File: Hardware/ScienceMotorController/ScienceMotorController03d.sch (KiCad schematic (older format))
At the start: 17 parts, among them U5 VNH5019A_E

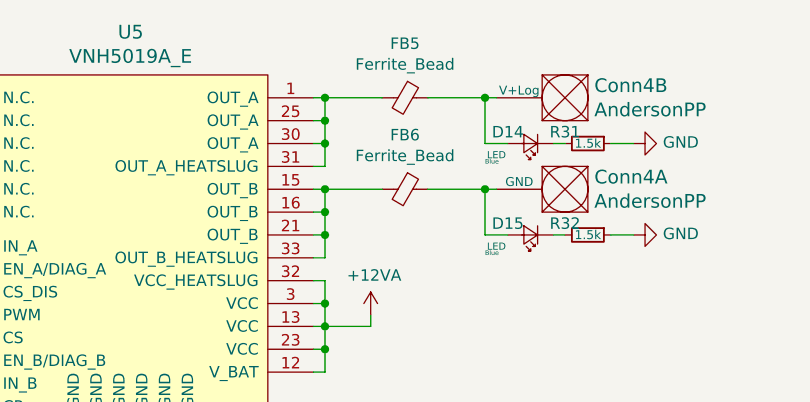
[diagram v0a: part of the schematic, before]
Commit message: finished assigning footprints, generated pcbnew
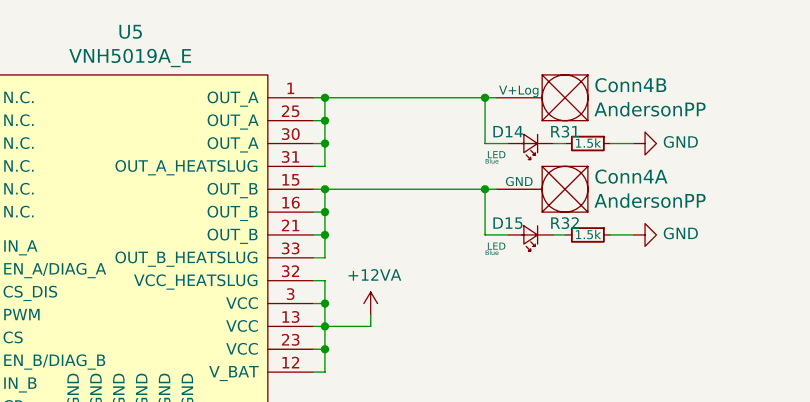
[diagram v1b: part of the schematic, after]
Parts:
- removed FB5, FB6: Ferrite_Bead, symbol Device:Ferrite_Bead_Small
- Conn4: footprint MRDT_Connectors:Anderson_2_Vertical_Sidy_by_Side -> MRDT_Connectors:Anderson_2_Horizontal_Side_by_Side
- U5: footprint (none) -> MRDT_ICs:MultiPowerSO_30
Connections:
- net at Conn4.2 (V+Log), D14.2 (A): now also U5.1 (OUT_A), U5.25 (OUT_A), U5.30 (OUT_A), U5.31 (OUT_A_HEATSLUG)
- net at Conn4.1 (GND), D15.2 (A): now also U5.15 (OUT_B), U5.16 (OUT_B), U5.21 (OUT_B), U5.33 (OUT_B_HEATSLUG)
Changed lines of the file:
@@
 F 0 "U5" H 5950 6187 60  0000 C CNN
 F 1 "VNH5019A_E" H 5950 6081 60  0000 C CNN
-F 2 "" H 5350 5800 60  0001 C CNN
+F 2 "MRDT_ICs:MultiPowerSO_30" H 5350 5800 60  0001 C CNN
 F 3 "" H 5350 5800 60  0001 C CNN
 	1    5350 4500
@@
 F 0 "Conn4" H 7922 3447 60  0000 R CNN
 F 1 "AndersonPP" H 7922 3553 60  0000 R CNN
-F 2 "MRDT_Connectors:Anderson_2_Vertical_Sidy_by_Side" H 7800 2850 60  0001 C CNN
+F 2 "MRDT_Connectors:Anderson_2_Horizontal_Side_by_Side" H 7800 2850 60  0001 C CNN
 F 3 "" H 7800 2850 60  0001 C CNN
 	1    7950 3400
@@
 F 0 "Conn4" H 7922 3047 60  0000 R CNN
 F 1 "AndersonPP" H 7922 3153 60  0000 R CNN
-F 2 "MRDT_Connectors:Anderson_2_Vertical_Sidy_by_Side" H 7800 2450 60  0001 C CNN
+F 2 "MRDT_Connectors:Anderson_2_Horizontal_Side_by_Side" H 7800 2450 60  0001 C CNN
 F 3 "" H 7800 2450 60  0001 C CNN
 	2    7950 3000
@@
 	5150 4150 4200 4150
 Connection ~ 4200 4150
-Wire Wire Line
-	7250 3100 7500 3100
-Wire Wire Line
-	7250 3500 7500 3500
 Wire Wire Line
 	7500 3300 7500 3100
@@
 	1    0    0    -1
 $EndComp
-$Comp
-L Device:Ferrite_Bead_Small FB?
-U 1 1 5F9ECC76
-P 7150 3100
-AR Path="/5F9082FC/5F9ECC76" Ref="FB?"  Part="1"
-AR Path="/5F7148FA/5FA34AD9/5F9ECC76" Ref="FB5"  Part="1"
-F 0 "FB5" V 6913 3100 50  0000 C CNN
-F 1 "Ferrite_Bead" V 7004 3100 50  0000 C CNN
-F 2 "" V 7080 3100 50  0001 C CNN
-F 3 "~" H 7150 3100 50  0001 C CNN
-	1    7150 3100
-	0    1    1    0
-$EndComp
-$Comp
-L Device:Ferrite_Bead_Small FB?
-U 1 1 5F9ED41C
-P 7150 3500
-AR Path="/5F9082FC/5F9ED41C" Ref="FB?"  Part="1"
-AR Path="/5F7148FA/5FA34AD9/5F9ED41C" Ref="FB6"  Part="1"
-F 0 "FB6" V 6913 3500 50  0000 C CNN
-F 1 "Ferrite_Bead" V 7004 3500 50  0000 C CNN
-F 2 "" V 7080 3500 50  0001 C CNN
-F 3 "~" H 7150 3500 50  0001 C CNN
-	1    7150 3500
-	0    1    1    0
-$EndComp
 Connection ~ 6800 3100
-Wire Wire Line
-	6800 3100 7050 3100
-Wire Wire Line
-	7050 3500 6800 3500
 Connection ~ 6800 3500
 Text HLabel 4700 3750 0    50   Input ~ 0
@@
 Text Notes 7500 3800 0    20   ~ 0
 Blue
+Wire Wire Line
+	6800 3500 7500 3500
+Wire Wire Line
+	6800 3100 7500 3100
 $EndSCHEMATC

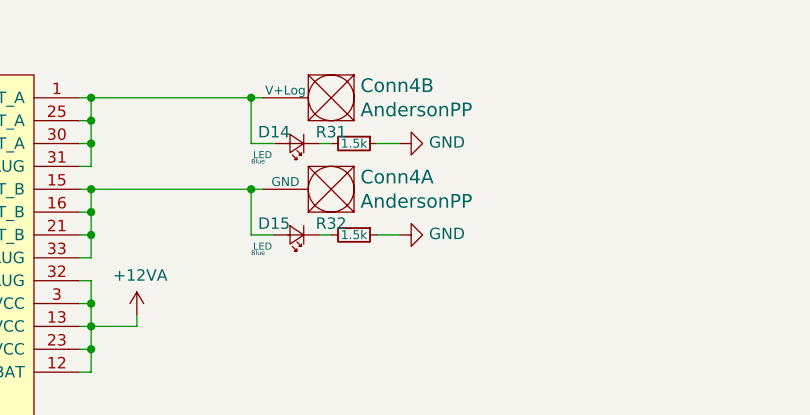
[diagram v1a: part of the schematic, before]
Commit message: running traces
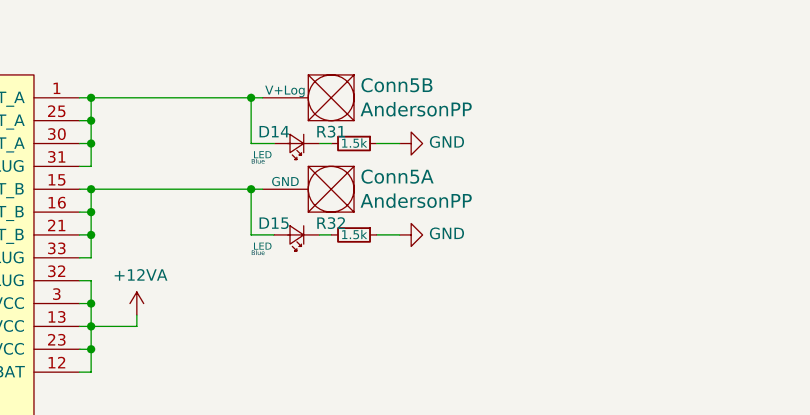
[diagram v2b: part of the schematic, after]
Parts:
- renumbered Conn4 to Conn5
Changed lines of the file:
@@
 AR Path="/5F7D111E/5FA6640B/5FA978B7" Ref="Conn?"  Part="1"
 AR Path="/5F9082FC/5FA978B7" Ref="Conn?"  Part="1"
-AR Path="/5F7148FA/5FA34AD9/5FA978B7" Ref="Conn4"  Part="1"
-F 0 "Conn4" H 7922 3447 60  0000 R CNN
+AR Path="/5F7148FA/5FA34AD9/5FA978B7" Ref="Conn5"  Part="1"
+F 0 "Conn5" H 7922 3447 60  0000 R CNN
 F 1 "AndersonPP" H 7922 3553 60  0000 R CNN
 F 2 "MRDT_Connectors:Anderson_2_Horizontal_Side_by_Side" H 7800 2850 60  0001 C CNN
@@
 AR Path="/5F7D111E/5FA6640B/5FA978BD" Ref="Conn?"  Part="2"
 AR Path="/5F9082FC/5FA978BD" Ref="Conn?"  Part="2"
-AR Path="/5F7148FA/5FA34AD9/5FA978BD" Ref="Conn4"  Part="2"
-F 0 "Conn4" H 7922 3047 60  0000 R CNN
+AR Path="/5F7148FA/5FA34AD9/5FA978BD" Ref="Conn5"  Part="2"
+F 0 "Conn5" H 7922 3047 60  0000 R CNN
 F 1 "AndersonPP" H 7922 3153 60  0000 R CNN
 F 2 "MRDT_Connectors:Anderson_2_Horizontal_Side_by_Side" H 7800 2450 60  0001 C CNN
